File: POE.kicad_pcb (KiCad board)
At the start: 2 copper layers, 42 x 70 mm, 22 parts, among them J1 RC01374, J2 Conn_01x02_Male

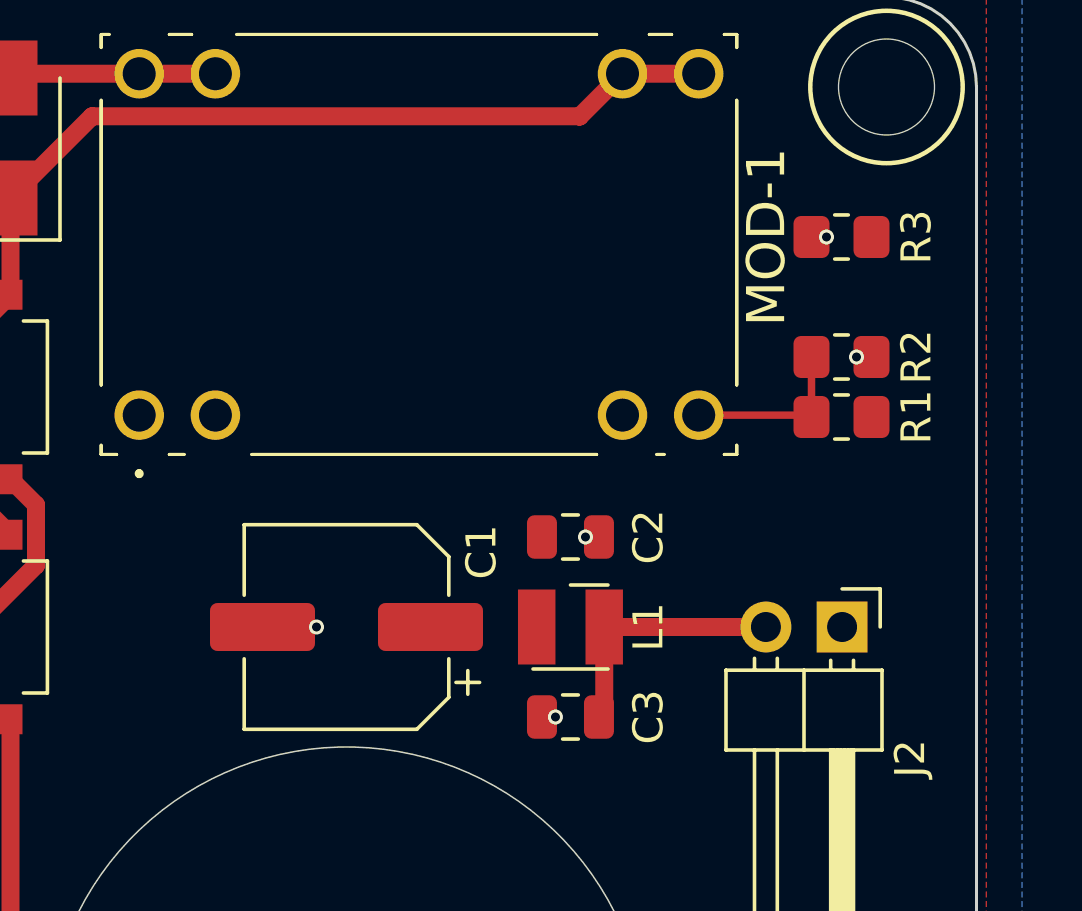
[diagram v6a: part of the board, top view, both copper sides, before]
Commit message: Post-test thoughts & adjustments.
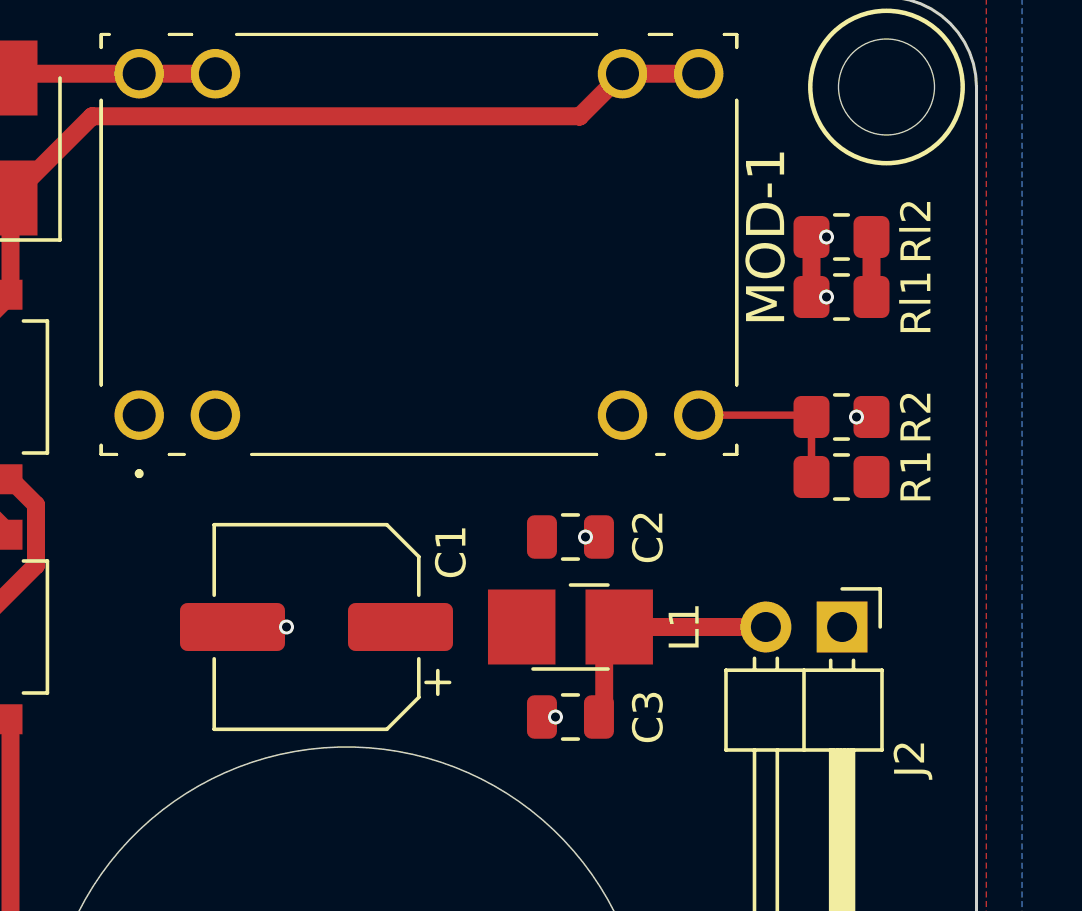
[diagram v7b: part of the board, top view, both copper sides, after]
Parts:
- added Rl2: Rmin, Resistor_SMD:R_0805_2012Metric_Pad1.20x1.40mm_HandSolder, F.Cu at (116.5, 73.0)
- moved R1 2.00 mm to (116.5, 81.0)
- moved R2 2.00 mm to (116.5, 79.0)
- moved Rl1 2.00 mm to (116.5, 75.0)
- moved C1 1.00 mm to (99.0, 86.0)
- renumbered R3 to Rl1
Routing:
- net Vout: track 0.00 -> 2.00 mm
- net GND: track 0.00 -> 2.00 mm, vias 6 -> 7
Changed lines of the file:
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@@
     (property "Sheetfile" "POE.kicad_sch")
     (property "Sheetname" "")
-    (property "exclude_from_bom" "")
-    (attr through_hole exclude_from_bom)
+    (attr through_hole)
     (fp_text reference "J1" (at -8.973903 6.497106 90 unlocked) (layer "F.SilkS")
       (effects (font (size 1 1) (thickness 0.15)))
@@
   )
   (footprint "Capacitor_SMD:CP_Elec_6.3x5.4" (layer "F.Cu")
-    (at 100 86 180)
+    (at 99 86 180)
     (descr "SMD capacitor, aluminum electrolytic, Panasonic C55, 6.3x5.4mm")
     (tags "capacitor electrolytic")
@@
     (property "Sheetname" "")
     (attr smd)
-    (fp_text reference "C1" (at -4.5 2.5 270) (layer "F.SilkS")
+    (fp_text reference "C1" (at -4.5 2.5 90) (layer "F.SilkS")
       (effects (font (size 1 1) (thickness 0.15)))
     )
-    (fp_text value "100uf" (at 0 4.35 180) (layer "F.Fab")
+    (fp_text value "100uf" (at 0 4.35) (layer "F.Fab")
       (effects (font (size 1 1) (thickness 0.15)))
     )
-    (fp_text user "${REFERENCE}" (at 0 0 180) (layer "F.Fab")
+    (fp_text user "${REFERENCE}" (at 0 0) (layer "F.Fab")
       (effects (font (size 1 1) (thickness 0.15)))
     )
@@
   )
   (footprint "Resistor_SMD:R_0805_2012Metric_Pad1.20x1.40mm_HandSolder" (layer "F.Cu")
-    (at 116.5 73 180)
+    (at 116.5 75 180)
     (descr "Resistor SMD 0805 (2012 Metric), square (rectangular) end terminal, IPC_7351 nominal with elongated pad for handsoldering. (Body size source: IPC-SM-782 page 72, https://www.pcb-3d.com/wordpress/wp-content/uploads/ipc-sm-782a_amendment_1_and_2.pdf), generated with kicad-footprint-generator")
     (tags "resistor handsolder")
     (property "Sheetfile" "POE.kicad_sch")
     (property "Sheetname" "")
-    (fp_text reference "R3" (at -2.5 0 90) (layer "F.SilkS")
+    (fp_text reference "Rl1" (at -2.5 -0.2 90) (layer "F.SilkS")
       (effects (font (size 1 1) (thickness 0.15)))
     )
@@
   )
   (footprint "Resistor_SMD:R_0805_2012Metric_Pad1.20x1.40mm_HandSolder" (layer "F.Cu")
-    (at 116.5 79 180)
+    (at 116.5 73 180)
+    (descr "Resistor SMD 0805 (2012 Metric), square (rectangular) end terminal, IPC_7351 nominal with elongated pad for handsoldering. (Body size source: IPC-SM-782 page 72, https://www.pcb-3d.com/wordpress/wp-content/uploads/ipc-sm-782a_amendment_1_and_2.pdf), generated with kicad-footprint-generator")
+    (tags "resistor handsolder")
+    (property "Sheetfile" "POE.kicad_sch")
+    (property "Sheetname" "")
+    (fp_text reference "Rl2" (at -2.5 0.2 90) (layer "F.SilkS")
+      (effects (font (size 1 1) (thickness 0.15)))
+    )
+    (fp_text value "Rmin" (at 0 1.65) (layer "F.Fab")
+      (effects (font (size 1 1) (thickness 0.15)))
+    )
+    (fp_text user "${REFERENCE}" (at 0 0) (layer "F.Fab")
+      (effects (font (size 0.5 0.5) (thickness 0.08)))
+    )
+    (fp_line (start -0.227064 0.735) (end 0.227064 0.735) (layer "F.SilkS") (width 0.12))
+    (fp_line (start -0.227064 -0.735) (end 0.227064 -0.735) (layer "F.SilkS") (width 0.12))
+    (fp_line (start -1.85 -0.95) (end 1.85 -0.95) (layer "F.CrtYd") (width 0.05))
+    (fp_line (start -1.85 0.95) (end -1.85 -0.95) (layer "F.CrtYd") (width 0.05))
+    (fp_line (start 1.85 -0.95) (end 1.85 0.95) (layer "F.CrtYd") (width 0.05))
+    (fp_line (start 1.85 0.95) (end -1.85 0.95) (layer "F.CrtYd") (width 0.05))
+    (fp_line (start 1 -0.625) (end 1 0.625) (layer "F.Fab") (width 0.1))
+    (fp_line (start -1 -0.625) (end 1 -0.625) (layer "F.Fab") (width 0.1))
+    (fp_line (start -1 0.625) (end -1 -0.625) (layer "F.Fab") (width 0.1))
+    (fp_line (start 1 0.625) (end -1 0.625) (layer "F.Fab") (width 0.1))
+    (pad "1" smd roundrect (at -1 0 180) (size 1.2 1.4) (layers "F.Cu" "F.Paste" "F.Mask") (roundrect_rratio 0.208333)
+      (net 1 "Vout") (pintype "passive"))
+    (pad "2" smd roundrect (at 1 0 180) (size 1.2 1.4) (layers "F.Cu" "F.Paste" "F.Mask") (roundrect_rratio 0.208333)
+      (net 2 "GND") (pintype "passive"))
+    (model "${KICAD6_3DMODEL_DIR}/Resistor_SMD.3dshapes/R_0805_2012Metric.wrl"
+      (offset (xyz 0 0 0))
+      (scale (xyz 1 1 1))
+      (rotate (xyz 0 0 0))
+    )
+  )
+  (footprint "Resistor_SMD:R_0805_2012Metric_Pad1.20x1.40mm_HandSolder" (layer "F.Cu")
+    (at 116.5 81 180)
     (descr "Resistor SMD 0805 (2012 Metric), square (rectangular) end terminal, IPC_7351 nominal with elongated pad for handsoldering. (Body size source: IPC-SM-782 page 72, https://www.pcb-3d.com/wordpress/wp-content/uploads/ipc-sm-782a_amendment_1_and_2.pdf), generated with kicad-footprint-generator")
     (tags "resistor handsolder")
@@
   )
   (footprint "Resistor_SMD:R_0805_2012Metric_Pad1.20x1.40mm_HandSolder" (layer "F.Cu")
-    (at 116.5 77)
+    (at 116.5 79)
     (descr "Resistor SMD 0805 (2012 Metric), square (rectangular) end terminal, IPC_7351 nominal with elongated pad for handsoldering. (Body size source: IPC-SM-782 page 72, https://www.pcb-3d.com/wordpress/wp-content/uploads/ipc-sm-782a_amendment_1_and_2.pdf), generated with kicad-footprint-generator")
     (tags "resistor handsolder")
@@
     (property "Sheetname" "")
     (attr smd)
-    (fp_text reference "L1" (at 2.6 0 90 unlocked) (layer "F.SilkS")
+    (fp_text reference "L1" (at 3.81 0 90 unlocked) (layer "F.SilkS")
       (effects (font (size 1 1) (thickness 0.15)))
     )
-    (fp_text value "fnr3015s1r" (at 0 2.1 unlocked) (layer "F.Fab")
+    (fp_text value "fnr3015s1r" (at 0 2.54 unlocked) (layer "F.Fab")
       (effects (font (size 1 1) (thickness 0.15)))
     )
@@
     (fp_line (start -0.75 -1) (end 1.25 -1) (layer "F.Fab") (width 0.1))
     (fp_line (start -0.75 -1) (end -1.25 -0.5) (layer "F.Fab") (width 0.1))
-    (pad "1" smd rect (at -1.125 0) (size 1.25 2.5) (layers "F.Cu" "F.Paste" "F.Mask")
+    (pad "1" smd rect (at -1.625 0) (size 2.25 2.5) (layers "F.Cu" "F.Paste" "F.Mask")
       (net 1 "Vout") (pinfunction "1") (pintype "passive"))
-    (pad "2" smd rect (at 1.125 0) (size 1.25 2.5) (layers "F.Cu" "F.Paste" "F.Mask")
+    (pad "2" smd rect (at 1.625 0) (size 2.25 2.5) (layers "F.Cu" "F.Paste" "F.Mask")
       (net 22 "VoutF") (pinfunction "2") (pintype "passive"))
     (model "${KICAD6_3DMODEL_DIR}/Inductor_SMD.3dshapes/L_Wuerth_MAPI-3015.wrl"
@@
     (effects (font (size 0.5 0.5) (thickness 0.1)))
   )
+  (segment (start 117.5 73) (end 117.5 75) (width 0.6) (layer "F.Cu") (net 1))
+  (segment (start 115.5 73) (end 115.5 75) (width 0.6) (layer "F.Cu") (net 2))
   (via (at 116 73) (size 0.5) (drill 0.3) (layers "F.Cu" "B.Cu") (net 2))
-  (via (at 117 77) (size 0.5) (drill 0.3) (layers "F.Cu" "B.Cu") (net 2))
+  (via (at 116 75) (size 0.5) (drill 0.3) (layers "F.Cu" "B.Cu") (net 2))
+  (via (at 117 79) (size 0.5) (drill 0.3) (layers "F.Cu" "B.Cu") (net 2))
   (via (at 107.965599 83) (size 0.5) (drill 0.3) (layers "F.Cu" "B.Cu") (net 2))
   (via (at 106.965599 89) (size 0.5) (drill 0.3) (layers "F.Cu" "B.Cu") (net 2))
   (via (at 116 122) (size 0.5) (drill 0.3) (layers "F.Cu" "B.Cu") (free) (net 2))
-  (via (at 99 86) (size 0.5) (drill 0.3) (layers "F.Cu" "B.Cu") (net 2))
+  (via (at 98 86) (size 0.5) (drill 0.3) (layers "F.Cu" "B.Cu") (net 2))
   (segment (start 111.740387 78.937467) (end 115.488553 78.937467) (width 0.25) (layer "F.Cu") (net 3))
-  (segment (start 115.5 79) (end 115.5 77) (width 0.25) (layer "F.Cu") (net 3))
+  (segment (start 115.5 81) (end 115.5 79) (width 0.25) (layer "F.Cu") (net 3))
   (segment (start 93.47462 113.844701) (end 103.634811 113.844701) (width 0.6) (layer "F.Cu") (net 4))
   (segment (start 86.26 81.075) (end 85.26 82.075) (width 0.6) (layer "F.Cu") (net 4))
